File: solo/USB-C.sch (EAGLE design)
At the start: 24 parts

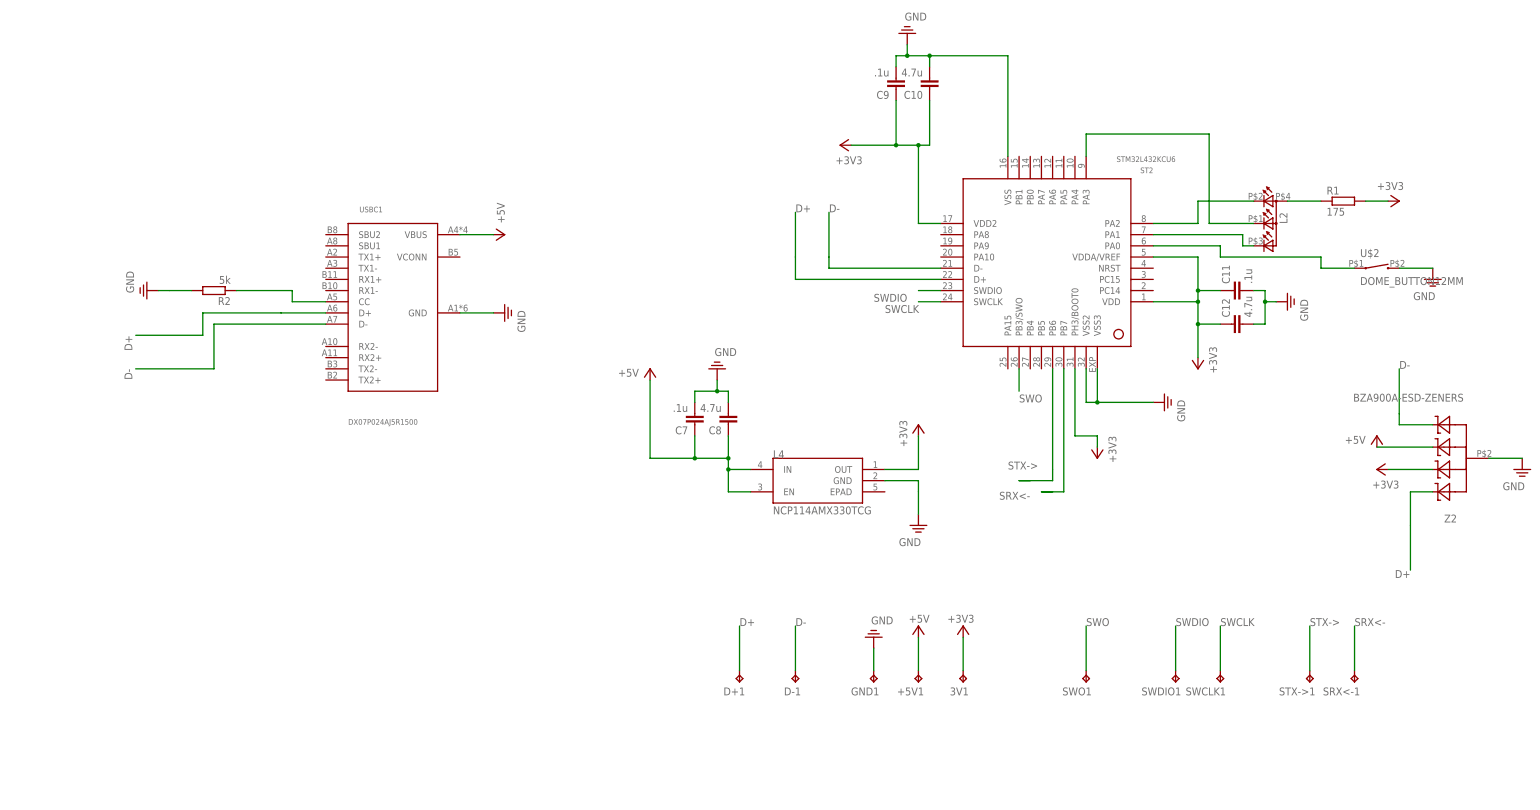
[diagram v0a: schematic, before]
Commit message: NFC designs
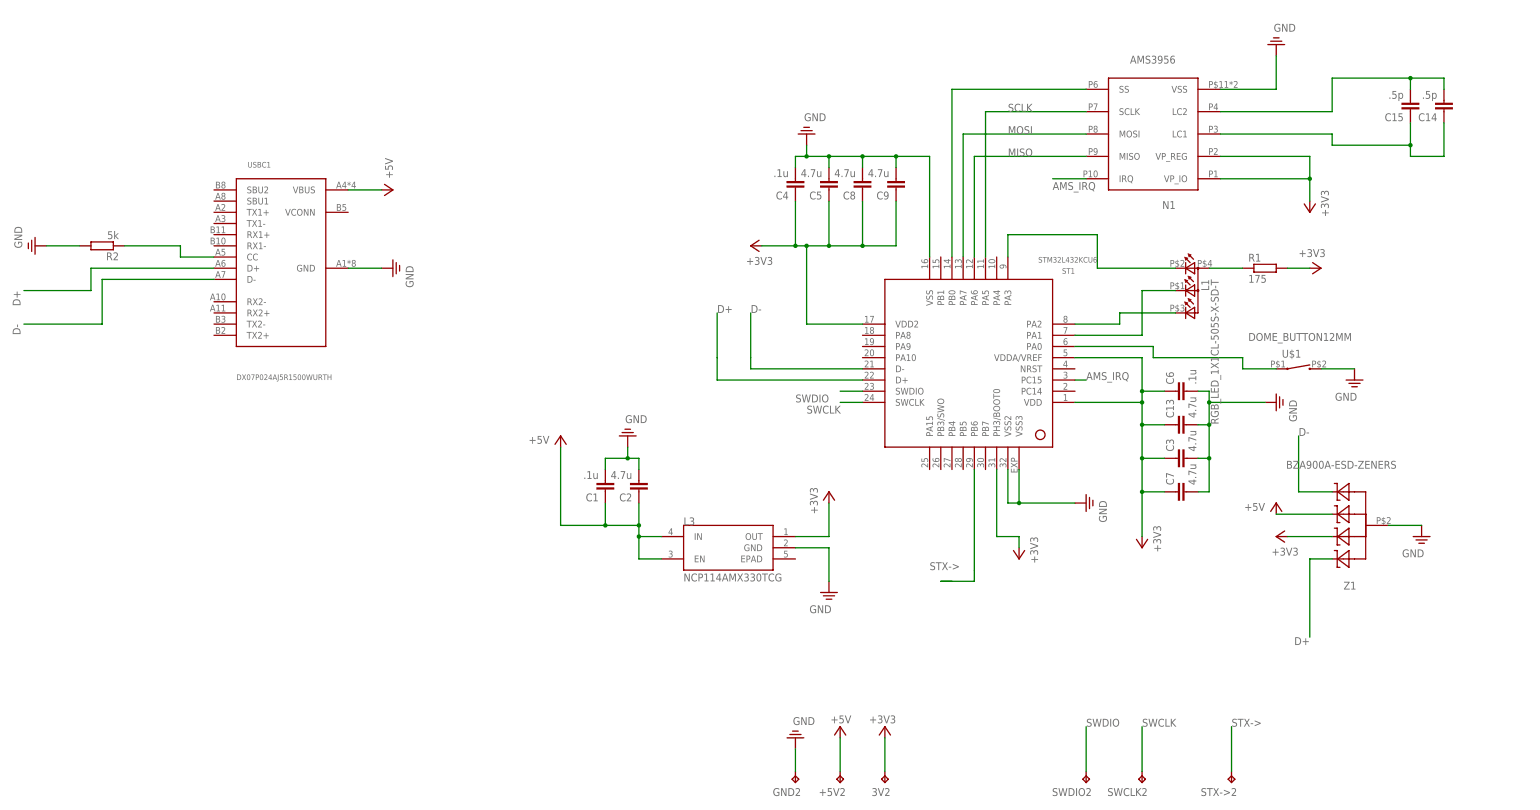
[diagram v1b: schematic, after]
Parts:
- removed +5V1, 3V1, D+1, D-1, GND1, SRX<-1, STX->1, SWCLK1, SWDIO1, SWO1: TEST_POINT, efm-fido:TEST_POINT
- removed C10, C12: 4.7u, efm-fido:CAPACITOR
- removed C11: .1u, efm-fido:CAPACITOR
- removed L2: EAST1616RGBA3-LED-RGBCL-505S-X-SD-T, efm-fido:EAST1616RGBA3-LED-RGBCL-505S-X-SD-T
- removed L4: NCP114AMX330TCG, efm-fido:NCP114AMX330TCG
- removed ST2: STM32L432KCU6, efm-fido:STM32L432KCU6
- removed U$2: DOME_BUTTON12MM, efm-fido:DOME_BUTTON12MM
- removed Z2: BZA900A-ESD-ZENERS, efm-fido:BZA900A-ESD-ZENERS
- added +5V2, 3V2, GND2, STX->2, SWCLK2, SWDIO2: TEST_POINT, efm-fido:TEST_POINT
- added C1, C4, C6: .1u, efm-fido:CAPACITOR
- added C13, C2, C3, C5: 4.7u, efm-fido:CAPACITOR
- added C14, C15: .5p, efm-fido:CAPACITOR
- added L1: RGB_LED_1X1CL-505S-X-SD-T, efm-fido:RGB_LED_1X1CL-505S-X-SD-T
- added L3: NCP114AMX330TCG, efm-fido:NCP114AMX330TCG
- added N1: AMS3956, efm-fido:AMS3956
- added ST1: STM32L432KCU6, efm-fido:STM32L432KCU6
- added U$1: DOME_BUTTON12MM, efm-fido:DOME_BUTTON12MM
- added Z1: BZA900A-ESD-ZENERS, efm-fido:BZA900A-ESD-ZENERS
- C7, C9: value .1u -> 4.7u
- USBC1: value DX07P024AJ5R1500 -> DX07P024AJ5R1500WURTH; device efm-fido:DX07P024AJ5R1500 -> efm-fido:DX07P024AJ5R1500WURTH
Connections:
- removed net N$10: L2.CBLUE, ST2.PA3
- removed net N$11: L2.CGREEN, ST2.PA1
- removed net N$12: ST2.PA0, U$2.1
- removed net SRX<-: SRX<-1.TP, ST2.PB7
- removed net SWO: ST2.PB3/SWO, SWO1.TP
- new net AMS_CS1: N1.SS, ST1.PB0
- new net AMS_IRQ: N1.IRQ, ST1.PC15
- new net MISO: N1.MISO, ST1.PA6
- new net MOSI: N1.MOSI, ST1.PA7
- new net N$2: L1.A2, R1.1
- new net N$3: L1.CGREEN, ST1.PA2
- new net N$4: L1.CRED, ST1.PA3
- new net N$5: L1.CBLUE, ST1.PA1
- new net N$6: ST1.PA0, U$1.1
- new net SCLK: N1.SCLK, ST1.PA5
- net +3V3: now also 3V2.TP, C13.1, C3.1, C4.1, C5.1, C6.1, C7.1, C8.1, L3.OUT, N1.VP_IO, N1.VP_REG, ST1.PH3/BOOT0, ST1.VDD, ST1.VDD2, ST1.VDDA/VREF, Z1.C1; no longer 3V1.TP, C10.1, C11.1, C12.1, L4.OUT, ST2.PH3/BOOT0, ST2.VDD, ST2.VDD2, ST2.VDDA/VREF, Z2.C1
- net +5V: now also +5V2.TP, C1.1, C2.1, L3.EN, L3.IN, Z1.C; no longer +5V1.TP, C7.1, C8.1, L4.EN, L4.IN, Z2.C
- net D+: now also ST1.D+, Z1.C3; no longer D+1.TP, ST2.D+, Z2.C3
- net D-: now also ST1.D-, Z1.C2; no longer D-1.TP, ST2.D-, Z2.C2
- net N$8: now also C14.2, C15.2, N1.LC2; no longer L2.A2, R1.1
- net N$9: now also C14.1, C15.1, N1.LC1; no longer L2.CRED, ST2.PA2
- net PE: now also C1.2, C13.2, C2.2, C3.2, C4.2, C5.2, C6.2, GND2.TP, L3.GND, N1.VSS, ST1.VSS, ST1.VSS2, ST1.VSS3, U$1.2, Z1.P$1; no longer C10.2, C11.2, C12.2, GND1.TP, L4.GND, ST2.VSS, ST2.VSS2, ST2.VSS3, U$2.2, Z2.P$1
- net STX->: now also ST1.PB6, STX->2.TP; no longer ST2.PB6, STX->1.TP
- net SWCLK: now also ST1.SWCLK, SWCLK2.TP; no longer ST2.SWCLK, SWCLK1.TP
- net SWDIO: now also ST1.SWDIO, SWDIO2.TP; no longer ST2.SWDIO, SWDIO1.TP
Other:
- moved on the sheet: C7, C8, C9, R1, R2, USBC1

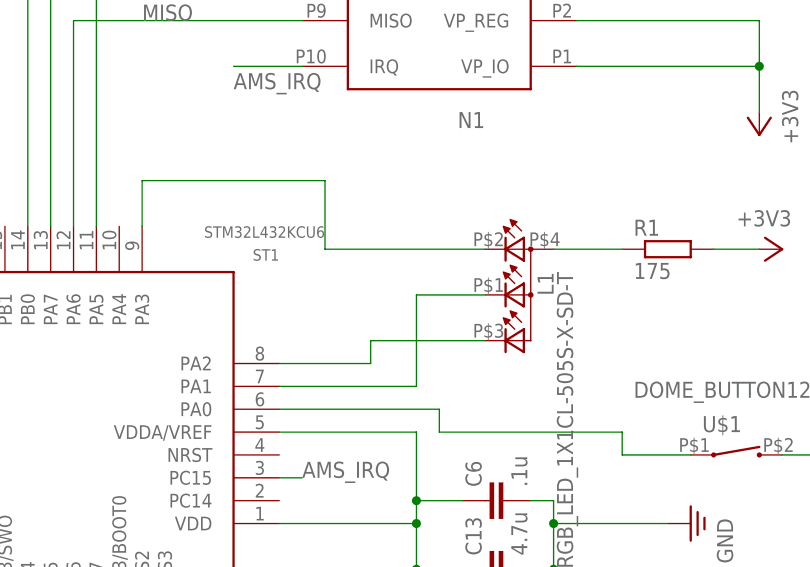
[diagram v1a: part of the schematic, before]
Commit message: go back to using old LED
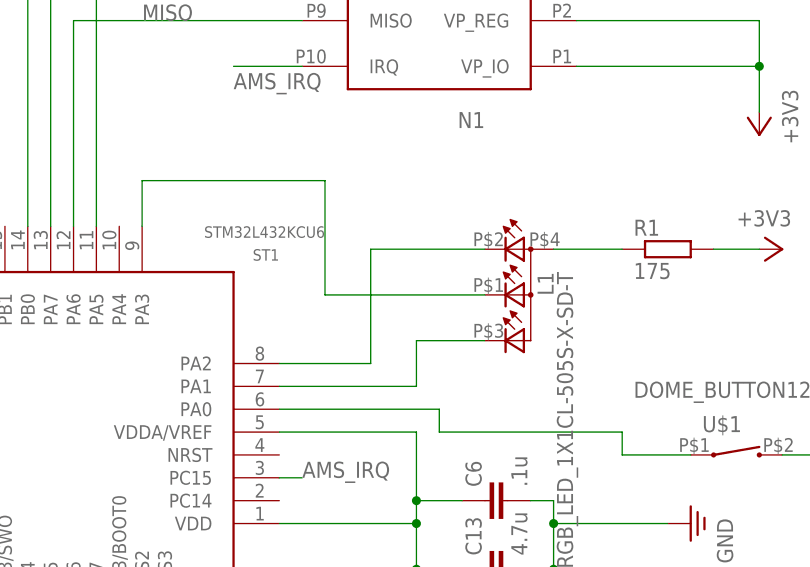
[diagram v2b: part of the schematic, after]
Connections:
- net N$3: now also L1.CRED; no longer L1.CGREEN
- net N$4: now also L1.CBLUE; no longer L1.CRED
- net N$5: now also L1.CGREEN; no longer L1.CBLUE
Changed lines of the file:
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@@
 <part name="C8" library="efm-fido" library_urn="urn:adsk.eagle:library:4245354" deviceset="CAPACITOR" device="" package3d_urn="urn:adsk.eagle:package:4245806/7" value="4.7u"/>
 <part name="C9" library="efm-fido" library_urn="urn:adsk.eagle:library:4245354" deviceset="CAPACITOR" device="" package3d_urn="urn:adsk.eagle:package:4245806/7" value="4.7u"/>
-<part name="L1" library="efm-fido" library_urn="urn:adsk.eagle:library:4245354" deviceset="RGB_LED_1X1" device="CL-505S-X-SD-T" package3d_urn="urn:adsk.eagle:package:4878740/7"/>
+<part name="L1" library="efm-fido" library_urn="urn:adsk.eagle:library:4245354" deviceset="RGB_LED_1X1" device="CL-505S-X-SD-T" package3d_urn="urn:adsk.eagle:package:4878740/8"/>
 </parts>
 <sheets>
@@
 <segment>
 <pinref part="ST1" gate="G$1" pin="PA2"/>
-<wire x1="154.94" y1="-2.54" x2="154.94" y2="-5.08" width="0.1524" layer="91"/>
 <wire x1="154.94" y1="-5.08" x2="144.78" y2="-5.08" width="0.1524" layer="91"/>
-<wire x1="167.64" y1="-2.54" x2="154.94" y2="-2.54" width="0.1524" layer="91"/>
-<pinref part="L1" gate="G$1" pin="CGREEN"/>
+<wire x1="154.94" y1="-5.08" x2="154.94" y2="7.62" width="0.1524" layer="91"/>
+<pinref part="L1" gate="G$1" pin="CRED"/>
+<wire x1="154.94" y1="7.62" x2="167.64" y2="7.62" width="0.1524" layer="91"/>
 </segment>
 </net>
@@
 <pinref part="ST1" gate="G$1" pin="PA3"/>
 <wire x1="129.54" y1="15.24" x2="129.54" y2="10.16" width="0.1524" layer="91"/>
-<pinref part="L1" gate="G$1" pin="CRED"/>
-<wire x1="167.64" y1="7.62" x2="149.86" y2="7.62" width="0.1524" layer="91"/>
-<wire x1="149.86" y1="7.62" x2="149.86" y2="15.24" width="0.1524" layer="91"/>
 <wire x1="149.86" y1="15.24" x2="129.54" y2="15.24" width="0.1524" layer="91"/>
+<pinref part="L1" gate="G$1" pin="CBLUE"/>
+<wire x1="149.86" y1="15.24" x2="149.86" y2="2.54" width="0.1524" layer="91"/>
+<wire x1="149.86" y1="2.54" x2="167.64" y2="2.54" width="0.1524" layer="91"/>
 </segment>
 </net>
@@
 <pinref part="ST1" gate="G$1" pin="PA1"/>
 <wire x1="144.78" y1="-7.62" x2="160.02" y2="-7.62" width="0.1524" layer="91"/>
-<pinref part="L1" gate="G$1" pin="CBLUE"/>
-<wire x1="167.64" y1="2.54" x2="160.02" y2="2.54" width="0.1524" layer="91"/>
-<wire x1="160.02" y1="2.54" x2="160.02" y2="-7.62" width="0.1524" layer="91"/>
-</segment>
-</net>
+<pinref part="L1" gate="G$1" pin="CGREEN"/>
+<wire x1="167.64" y1="-2.54" x2="160.02" y2="-2.54" width="0.1524" layer="91"/>
+<wire x1="160.02" y1="-2.54" x2="160.02" y2="-7.62" width="0.1524" layer="91"/>
+</segment>
+</net>
